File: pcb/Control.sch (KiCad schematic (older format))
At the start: 23 parts, among them SW1 Pulsador_2p, U1 ATMEGA328, U2 PCA9685, U3 FT231X, Y1 16MHz

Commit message: añadidos led para estado y alimentacion externa para salidas digitales
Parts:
- added D33, D34, D35: Rojo, Leds:LED_0805, symbol LED
- added R49, R50, R51: 270, Resistors_SMD:R_0805, symbol R
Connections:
- net +5V: now also D33.2 (A), D34.2 (A), D35.2 (A)
- net MISO: now also R50.1
- net MOSI: now also R49.1
- net SCK: now also R51.1
- new net: D33.1 (K), R49.2
- new net: D34.1 (K), R50.2
- new net: D35.1 (K), R51.2
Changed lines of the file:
@@
 Text GLabel 4250 3550 2    60   BiDi ~ 0
 MISO
-Text GLabel 4250 3650 2    60   Input ~ 0
+Text GLabel 4250 3650 2    60   BiDi ~ 0
 SCK
 Wire Wire Line
@@
 	1    0    0    -1
 $EndComp
+$Comp
+L LED D33
+U 1 1 57B391B3
+P 9500 5400
+F 0 "D33" V 9500 5600 50  0000 R CNN
+F 1 "Rojo" H 9750 5350 50  0000 R CNN
+F 2 "Leds:LED_0805" H 9500 5400 50  0001 C CNN
+F 3 "" H 9500 5400 50  0000 C CNN
+F 4 "KINGBRIGHT ELECTRONIC" H 1200 3750 60  0001 C CNN "Fabricante"
+F 5 "KP-2012EC" H 1200 3750 60  0001 C CNN "Ref"
+F 6 "~" H 1200 3750 60  0001 C CNN "Potencia"
+F 7 "~" H 1200 3750 60  0001 C CNN "Tolerancia"
+F 8 "tme" H 1200 3750 60  0001 C CNN "Provedor"
+F 9 "KP-2012EC" H 1200 3750 60  0001 C CNN "Ref_Proveedor"
+	1    9500 5400
+	0    -1   -1   0
+$EndComp
+$Comp
+L LED D34
+U 1 1 57B391C0
+P 9800 5400
+F 0 "D34" V 9800 5600 50  0000 R CNN
+F 1 "Rojo" H 10050 5350 50  0000 R CNN
+F 2 "Leds:LED_0805" H 9800 5400 50  0001 C CNN
+F 3 "" H 9800 5400 50  0000 C CNN
+F 4 "KINGBRIGHT ELECTRONIC" H 1300 3750 60  0001 C CNN "Fabricante"
+F 5 "KP-2012EC" H 1300 3750 60  0001 C CNN "Ref"
+F 6 "~" H 1300 3750 60  0001 C CNN "Potencia"
+F 7 "~" H 1300 3750 60  0001 C CNN "Tolerancia"
+F 8 "tme" H 1300 3750 60  0001 C CNN "Provedor"
+F 9 "KP-2012EC" H 1300 3750 60  0001 C CNN "Ref_Proveedor"
+	1    9800 5400
+	0    -1   -1   0
+$EndComp
+Wire Wire Line
+	9800 5600 9800 5900
+Wire Wire Line
+	9500 5800 9500 5600
+$Comp
+L +5V #PWR018
+U 1 1 57B391C9
+P 9500 4950
+F 0 "#PWR018" H 9500 4800 50  0001 C CNN
+F 1 "+5V" H 9515 5123 50  0000 C CNN
+F 2 "" H 9500 4950 50  0000 C CNN
+F 3 "" H 9500 4950 50  0000 C CNN
+	1    9500 4950
+	1    0    0    -1
+$EndComp
+$Comp
+L +5V #PWR019
+U 1 1 57B391CF
+P 9800 4950
+F 0 "#PWR019" H 9800 4800 50  0001 C CNN
+F 1 "+5V" H 9815 5123 50  0000 C CNN
+F 2 "" H 9800 4950 50  0000 C CNN
+F 3 "" H 9800 4950 50  0000 C CNN
+	1    9800 4950
+	1    0    0    -1
+$EndComp
+Wire Wire Line
+	9800 4950 9800 5200
+Wire Wire Line
+	9500 4950 9500 5200
+$Comp
+L R R50
+U 1 1 57B3920F
+P 8900 5900
+F 0 "R50" V 8950 5700 50  0000 C CNN
+F 1 "270" V 8900 5900 50  0000 C CNN
+F 2 "Resistors_SMD:R_0805" V 8830 5900 50  0001 C CNN
+F 3 "" H 8900 5900 50  0000 C CNN
+F 4 "vishay" H 1150 3850 60  0001 C CNN "Fabricante"
+F 5 "CRCW0805270RFKTABC" H 1150 3850 60  0001 C CNN "Ref"
+F 6 "~" H 1150 3850 60  0001 C CNN "Potencia"
+F 7 "~" H 1150 3850 60  0001 C CNN "Tolerancia"
+F 8 "tme" H 1150 3850 60  0001 C CNN "Provedor"
+F 9 "CRCW0805270RFKTABC" H 1150 3850 60  0001 C CNN "Ref_Proveedor"
+	1    8900 5900
+	0    -1   -1   0
+$EndComp
+$Comp
+L R R49
+U 1 1 57B3937B
+P 8550 5800
+F 0 "R49" V 8600 5600 50  0000 C CNN
+F 1 "270" V 8550 5800 50  0000 C CNN
+F 2 "Resistors_SMD:R_0805" V 8480 5800 50  0001 C CNN
+F 3 "" H 8550 5800 50  0000 C CNN
+F 4 "vishay" H 800 3750 60  0001 C CNN "Fabricante"
+F 5 "CRCW0805270RFKTABC" H 800 3750 60  0001 C CNN "Ref"
+F 6 "~" H 800 3750 60  0001 C CNN "Potencia"
+F 7 "~" H 800 3750 60  0001 C CNN "Tolerancia"
+F 8 "tme" H 800 3750 60  0001 C CNN "Provedor"
+F 9 "CRCW0805270RFKTABC" H 800 3750 60  0001 C CNN "Ref_Proveedor"
+	1    8550 5800
+	0    -1   -1   0
+$EndComp
+Wire Wire Line
+	8700 5800 9500 5800
+Wire Wire Line
+	9800 5900 9050 5900
+Text GLabel 8100 5800 0    60   BiDi ~ 0
+MOSI
+Text GLabel 8100 5900 0    60   BiDi ~ 0
+MISO
+Wire Wire Line
+	8100 5900 8750 5900
+Wire Wire Line
+	8400 5800 8100 5800
+$Comp
+L LED D35
+U 1 1 57B39D33
+P 10100 5400
+F 0 "D35" V 10100 5600 50  0000 R CNN
+F 1 "Rojo" H 10350 5350 50  0000 R CNN
+F 2 "Leds:LED_0805" H 10100 5400 50  0001 C CNN
+F 3 "" H 10100 5400 50  0000 C CNN
+F 4 "KINGBRIGHT ELECTRONIC" H 1600 3750 60  0001 C CNN "Fabricante"
+F 5 "KP-2012EC" H 1600 3750 60  0001 C CNN "Ref"
+F 6 "~" H 1600 3750 60  0001 C CNN "Potencia"
+F 7 "~" H 1600 3750 60  0001 C CNN "Tolerancia"
+F 8 "tme" H 1600 3750 60  0001 C CNN "Provedor"
+F 9 "KP-2012EC" H 1600 3750 60  0001 C CNN "Ref_Proveedor"
+	1    10100 5400
+	0    -1   -1   0
+$EndComp
+Wire Wire Line
+	10100 5600 10100 6000
+$Comp
+L +5V #PWR020
+U 1 1 57B39D3B
+P 10100 4950
+F 0 "#PWR020" H 10100 4800 50  0001 C CNN
+F 1 "+5V" H 10115 5123 50  0000 C CNN
+F 2 "" H 10100 4950 50  0000 C CNN
+F 3 "" H 10100 4950 50  0000 C CNN
+	1    10100 4950
+	1    0    0    -1
+$EndComp
+Wire Wire Line
+	10100 4950 10100 5200
+$Comp
+L R R51
+U 1 1 57B3A35F
+P 9250 6000
+F 0 "R51" V 9300 5800 50  0000 C CNN
+F 1 "270" V 9250 6000 50  0000 C CNN
+F 2 "Resistors_SMD:R_0805" V 9180 6000 50  0001 C CNN
+F 3 "" H 9250 6000 50  0000 C CNN
+F 4 "vishay" H 1500 3950 60  0001 C CNN "Fabricante"
+F 5 "CRCW0805270RFKTABC" H 1500 3950 60  0001 C CNN "Ref"
+F 6 "~" H 1500 3950 60  0001 C CNN "Potencia"
+F 7 "~" H 1500 3950 60  0001 C CNN "Tolerancia"
+F 8 "tme" H 1500 3950 60  0001 C CNN "Provedor"
+F 9 "CRCW0805270RFKTABC" H 1500 3950 60  0001 C CNN "Ref_Proveedor"
+	1    9250 6000
+	0    -1   -1   0
+$EndComp
+Text GLabel 8100 6000 0    60   BiDi ~ 0
+SCK
+Wire Wire Line
+	8100 6000 9100 6000
+Wire Wire Line
+	10100 6000 9400 6000
 $EndSCHEMATC

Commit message: añadir imagenes y datos al esquema electrico
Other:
- moved on the sheet: C1, C2, R1, R5, R6, SW1, U1, Y1

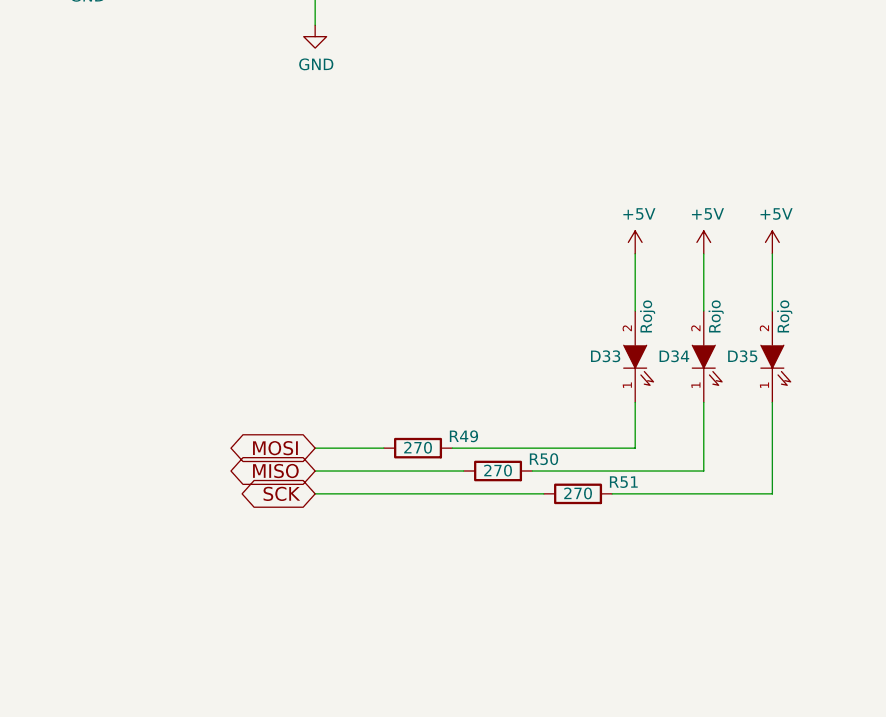
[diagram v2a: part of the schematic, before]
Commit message: correcciones menores y ecualizar longitud de pistas
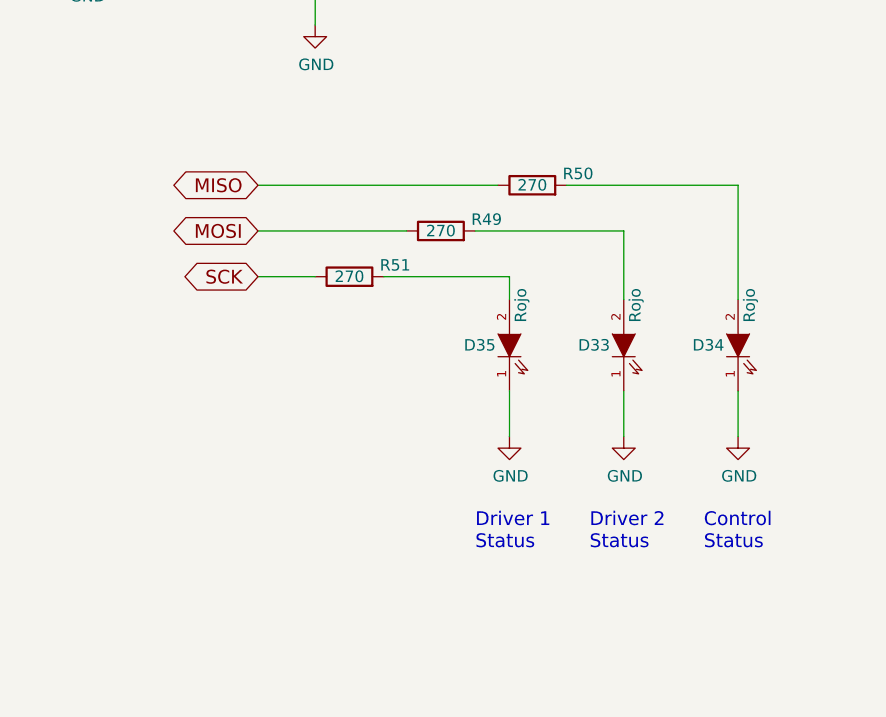
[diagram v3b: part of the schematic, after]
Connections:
- net +5V: no longer D33.2 (A), D34.2 (A), D35.2 (A)
- net GND: now also D33.1 (K), D34.1 (K), D35.1 (K)
- net at R49.2: now also D33.2 (A); no longer D33.1 (K)
- net at R50.2: now also D34.2 (A); no longer D34.1 (K)
- net at R51.2: now also D35.2 (A); no longer D35.1 (K)
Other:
- note added: "Control \nStatus"
- note added: "Driver 1 \nStatus"
- note added: "Driver 2 \nStatus"
- moved on the sheet: D33, D34, D35, R49, R50, R51
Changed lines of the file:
@@
-$EndComp
-$Comp
-L LED D33
-U 1 1 57B391B3
-P 9500 5400
-F 0 "D33" V 9500 5600 50  0000 R CNN
-F 1 "Rojo" H 9750 5350 50  0000 R CNN
-F 2 "Leds:LED_0805" H 9500 5400 50  0001 C CNN
-F 3 "" H 9500 5400 50  0000 C CNN
-F 4 "KINGBRIGHT ELECTRONIC" H 1200 3750 60  0001 C CNN "Fabricante"
-F 5 "KP-2012EC" H 1200 3750 60  0001 C CNN "Ref"
-F 6 "~" H 1200 3750 60  0001 C CNN "Potencia"
-F 7 "~" H 1200 3750 60  0001 C CNN "Tolerancia"
-F 8 "tme" H 1200 3750 60  0001 C CNN "Provedor"
-F 9 "KP-2012EC" H 1200 3750 60  0001 C CNN "Ref_Proveedor"
-	1    9500 5400
-	0    -1   -1   0
 $EndComp
 $Comp
 L LED D34
 U 1 1 57B391C0
-P 9800 5400
-F 0 "D34" V 9800 5600 50  0000 R CNN
-F 1 "Rojo" H 10050 5350 50  0000 R CNN
-F 2 "Leds:LED_0805" H 9800 5400 50  0001 C CNN
-F 3 "" H 9800 5400 50  0000 C CNN
-F 4 "KINGBRIGHT ELECTRONIC" H 1300 3750 60  0001 C CNN "Fabricante"
-F 5 "KP-2012EC" H 1300 3750 60  0001 C CNN "Ref"
-F 6 "~" H 1300 3750 60  0001 C CNN "Potencia"
-F 7 "~" H 1300 3750 60  0001 C CNN "Tolerancia"
-F 8 "tme" H 1300 3750 60  0001 C CNN "Provedor"
-F 9 "KP-2012EC" H 1300 3750 60  0001 C CNN "Ref_Proveedor"
-	1    9800 5400
+P 9950 5350
+F 0 "D34" V 9950 5550 50  0000 R CNN
+F 1 "Rojo" H 10200 5300 50  0000 R CNN
+F 2 "Leds:LED_0805" H 9950 5350 50  0001 C CNN
+F 3 "" H 9950 5350 50  0000 C CNN
+F 4 "KINGBRIGHT ELECTRONIC" H 1450 3700 60  0001 C CNN "Fabricante"
+F 5 "KP-2012EC" H 1450 3700 60  0001 C CNN "Ref"
+F 6 "~" H 1450 3700 60  0001 C CNN "Potencia"
+F 7 "~" H 1450 3700 60  0001 C CNN "Tolerancia"
+F 8 "tme" H 1450 3700 60  0001 C CNN "Provedor"
+F 9 "KP-2012EC" H 1450 3700 60  0001 C CNN "Ref_Proveedor"
+	1    9950 5350
 	0    -1   -1   0
 $EndComp
-Wire Wire Line
-	9800 5600 9800 5900
-Wire Wire Line
-	9500 5800 9500 5600
-$Comp
-L +5V #PWR018
-U 1 1 57B391C9
-P 9500 4950
-F 0 "#PWR018" H 9500 4800 50  0001 C CNN
-F 1 "+5V" H 9515 5123 50  0000 C CNN
-F 2 "" H 9500 4950 50  0000 C CNN
-F 3 "" H 9500 4950 50  0000 C CNN
-	1    9500 4950
-	1    0    0    -1
-$EndComp
-$Comp
-L +5V #PWR019
-U 1 1 57B391CF
-P 9800 4950
-F 0 "#PWR019" H 9800 4800 50  0001 C CNN
-F 1 "+5V" H 9815 5123 50  0000 C CNN
-F 2 "" H 9800 4950 50  0000 C CNN
-F 3 "" H 9800 4950 50  0000 C CNN
-	1    9800 4950
-	1    0    0    -1
-$EndComp
-Wire Wire Line
-	9800 4950 9800 5200
-Wire Wire Line
-	9500 4950 9500 5200
 $Comp
 L R R50
 U 1 1 57B3920F
-P 8900 5900
-F 0 "R50" V 8950 5700 50  0000 C CNN
-F 1 "270" V 8900 5900 50  0000 C CNN
-F 2 "Resistors_SMD:R_0805" V 8830 5900 50  0001 C CNN
-F 3 "" H 8900 5900 50  0000 C CNN
-F 4 "vishay" H 1150 3850 60  0001 C CNN "Fabricante"
-F 5 "CRCW0805270RFKTABC" H 1150 3850 60  0001 C CNN "Ref"
-F 6 "~" H 1150 3850 60  0001 C CNN "Potencia"
-F 7 "~" H 1150 3850 60  0001 C CNN "Tolerancia"
-F 8 "tme" H 1150 3850 60  0001 C CNN "Provedor"
-F 9 "CRCW0805270RFKTABC" H 1150 3850 60  0001 C CNN "Ref_Proveedor"
-	1    8900 5900
+P 9050 4650
+F 0 "R50" V 9100 4450 50  0000 C CNN
+F 1 "270" V 9050 4650 50  0000 C CNN
+F 2 "Resistors_SMD:R_0805" V 8980 4650 50  0001 C CNN
+F 3 "" H 9050 4650 50  0000 C CNN
+F 4 "vishay" H 1300 2600 60  0001 C CNN "Fabricante"
+F 5 "CRCW0805270RFKTABC" H 1300 2600 60  0001 C CNN "Ref"
+F 6 "~" H 1300 2600 60  0001 C CNN "Potencia"
+F 7 "~" H 1300 2600 60  0001 C CNN "Tolerancia"
+F 8 "tme" H 1300 2600 60  0001 C CNN "Provedor"
+F 9 "CRCW0805270RFKTABC" H 1300 2600 60  0001 C CNN "Ref_Proveedor"
+	1    9050 4650
 	0    -1   -1   0
 $EndComp
@@
 L R R49
 U 1 1 57B3937B
-P 8550 5800
-F 0 "R49" V 8600 5600 50  0000 C CNN
-F 1 "270" V 8550 5800 50  0000 C CNN
-F 2 "Resistors_SMD:R_0805" V 8480 5800 50  0001 C CNN
-F 3 "" H 8550 5800 50  0000 C CNN
-F 4 "vishay" H 800 3750 60  0001 C CNN "Fabricante"
-F 5 "CRCW0805270RFKTABC" H 800 3750 60  0001 C CNN "Ref"
-F 6 "~" H 800 3750 60  0001 C CNN "Potencia"
-F 7 "~" H 800 3750 60  0001 C CNN "Tolerancia"
-F 8 "tme" H 800 3750 60  0001 C CNN "Provedor"
-F 9 "CRCW0805270RFKTABC" H 800 3750 60  0001 C CNN "Ref_Proveedor"
-	1    8550 5800
+P 8650 4850
+F 0 "R49" V 8700 4650 50  0000 C CNN
+F 1 "270" V 8650 4850 50  0000 C CNN
+F 2 "Resistors_SMD:R_0805" V 8580 4850 50  0001 C CNN
+F 3 "" H 8650 4850 50  0000 C CNN
+F 4 "vishay" H 900 2800 60  0001 C CNN "Fabricante"
+F 5 "CRCW0805270RFKTABC" H 900 2800 60  0001 C CNN "Ref"
+F 6 "~" H 900 2800 60  0001 C CNN "Potencia"
+F 7 "~" H 900 2800 60  0001 C CNN "Tolerancia"
+F 8 "tme" H 900 2800 60  0001 C CNN "Provedor"
+F 9 "CRCW0805270RFKTABC" H 900 2800 60  0001 C CNN "Ref_Proveedor"
+	1    8650 4850
 	0    -1   -1   0
 $EndComp
-Wire Wire Line
-	8700 5800 9500 5800
-Wire Wire Line
-	9800 5900 9050 5900
-Text GLabel 8100 5800 0    60   BiDi ~ 0
+Text GLabel 7850 4850 0    60   BiDi ~ 0
 MOSI
-Text GLabel 8100 5900 0    60   BiDi ~ 0
+Text GLabel 7850 4650 0    60   BiDi ~ 0
 MISO
 Wire Wire Line
-	8100 5900 8750 5900
-Wire Wire Line
-	8400 5800 8100 5800
+	7850 4650 8900 4650
 $Comp
 L LED D35
 U 1 1 57B39D33
-P 10100 5400
-F 0 "D35" V 10100 5600 50  0000 R CNN
-F 1 "Rojo" H 10350 5350 50  0000 R CNN
-F 2 "Leds:LED_0805" H 10100 5400 50  0001 C CNN
-F 3 "" H 10100 5400 50  0000 C CNN
-F 4 "KINGBRIGHT ELECTRONIC" H 1600 3750 60  0001 C CNN "Fabricante"
-F 5 "KP-2012EC" H 1600 3750 60  0001 C CNN "Ref"
-F 6 "~" H 1600 3750 60  0001 C CNN "Potencia"
-F 7 "~" H 1600 3750 60  0001 C CNN "Tolerancia"
-F 8 "tme" H 1600 3750 60  0001 C CNN "Provedor"
-F 9 "KP-2012EC" H 1600 3750 60  0001 C CNN "Ref_Proveedor"
-	1    10100 5400
+P 8950 5350
+F 0 "D35" V 8950 5550 50  0000 R CNN
+F 1 "Rojo" H 9200 5300 50  0000 R CNN
+F 2 "Leds:LED_0805" H 8950 5350 50  0001 C CNN
+F 3 "" H 8950 5350 50  0000 C CNN
+F 4 "KINGBRIGHT ELECTRONIC" H 450 3700 60  0001 C CNN "Fabricante"
+F 5 "KP-2012EC" H 450 3700 60  0001 C CNN "Ref"
+F 6 "~" H 450 3700 60  0001 C CNN "Potencia"
+F 7 "~" H 450 3700 60  0001 C CNN "Tolerancia"
+F 8 "tme" H 450 3700 60  0001 C CNN "Provedor"
+F 9 "KP-2012EC" H 450 3700 60  0001 C CNN "Ref_Proveedor"
+	1    8950 5350
 	0    -1   -1   0
 $EndComp
-Wire Wire Line
-	10100 5600 10100 6000
-$Comp
-L +5V #PWR020
-U 1 1 57B39D3B
-P 10100 4950
-F 0 "#PWR020" H 10100 4800 50  0001 C CNN
-F 1 "+5V" H 10115 5123 50  0000 C CNN
-F 2 "" H 10100 4950 50  0000 C CNN
-F 3 "" H 10100 4950 50  0000 C CNN
-	1    10100 4950
-	1    0    0    -1
-$EndComp
-Wire Wire Line
-	10100 4950 10100 5200
 $Comp
 L R R51
 U 1 1 57B3A35F
-P 9250 6000
-F 0 "R51" V 9300 5800 50  0000 C CNN
-F 1 "270" V 9250 6000 50  0000 C CNN
-F 2 "Resistors_SMD:R_0805" V 9180 6000 50  0001 C CNN
-F 3 "" H 9250 6000 50  0000 C CNN
-F 4 "vishay" H 1500 3950 60  0001 C CNN "Fabricante"
-F 5 "CRCW0805270RFKTABC" H 1500 3950 60  0001 C CNN "Ref"
-F 6 "~" H 1500 3950 60  0001 C CNN "Potencia"
-F 7 "~" H 1500 3950 60  0001 C CNN "Tolerancia"
-F 8 "tme" H 1500 3950 60  0001 C CNN "Provedor"
-F 9 "CRCW0805270RFKTABC" H 1500 3950 60  0001 C CNN "Ref_Proveedor"
-	1    9250 6000
+P 8250 5050
+F 0 "R51" V 8300 4850 50  0000 C CNN
+F 1 "270" V 8250 5050 50  0000 C CNN
+F 2 "Resistors_SMD:R_0805" V 8180 5050 50  0001 C CNN
+F 3 "" H 8250 5050 50  0000 C CNN
+F 4 "vishay" H 500 3000 60  0001 C CNN "Fabricante"
+F 5 "CRCW0805270RFKTABC" H 500 3000 60  0001 C CNN "Ref"
+F 6 "~" H 500 3000 60  0001 C CNN "Potencia"
+F 7 "~" H 500 3000 60  0001 C CNN "Tolerancia"
+F 8 "tme" H 500 3000 60  0001 C CNN "Provedor"
+F 9 "CRCW0805270RFKTABC" H 500 3000 60  0001 C CNN "Ref_Proveedor"
+	1    8250 5050
 	0    -1   -1   0
 $EndComp
-Text GLabel 8100 6000 0    60   BiDi ~ 0
+Text GLabel 7850 5050 0    60   BiDi ~ 0
 SCK
-Wire Wire Line
-	8100 6000 9100 6000
-Wire Wire Line
-	10100 6000 9400 6000
 $Bitmap
 Pos 10900 6850
@@
 EndData
 $EndBitmap
+Wire Wire Line
+	8100 5050 7850 5050
+$Comp
+L LED D33
+U 1 1 57B391B3
+P 9450 5350
+F 0 "D33" V 9450 5550 50  0000 R CNN
+F 1 "Rojo" H 9700 5300 50  0000 R CNN
+F 2 "Leds:LED_0805" H 9450 5350 50  0001 C CNN
+F 3 "" H 9450 5350 50  0000 C CNN
+F 4 "KINGBRIGHT ELECTRONIC" H 1150 3700 60  0001 C CNN "Fabricante"
+F 5 "KP-2012EC" H 1150 3700 60  0001 C CNN "Ref"
+F 6 "~" H 1150 3700 60  0001 C CNN "Potencia"
+F 7 "~" H 1150 3700 60  0001 C CNN "Tolerancia"
+F 8 "tme" H 1150 3700 60  0001 C CNN "Provedor"
+F 9 "KP-2012EC" H 1150 3700 60  0001 C CNN "Ref_Proveedor"
+	1    9450 5350
+	0    -1   -1   0
+$EndComp
+$Comp
+L GND #PWR018
+U 1 1 57B5BB38
+P 9450 5750
+F 0 "#PWR018" H 9450 5500 50  0001 C CNN
+F 1 "GND" H 9455 5577 50  0000 C CNN
+F 2 "" H 9450 5750 50  0000 C CNN
+F 3 "" H 9450 5750 50  0000 C CNN
+	1    9450 5750
+	1    0    0    -1
+$EndComp
+$Comp
+L GND #PWR019
+U 1 1 57B5BBA1
+P 9950 5750
+F 0 "#PWR019" H 9950 5500 50  0001 C CNN
+F 1 "GND" H 9955 5577 50  0000 C CNN
+F 2 "" H 9950 5750 50  0000 C CNN
+F 3 "" H 9950 5750 50  0000 C CNN
+	1    9950 5750
+	1    0    0    -1
+$EndComp
+$Comp
+L GND #PWR020
+U 1 1 57B5BC03
+P 8950 5750
+F 0 "#PWR020" H 8950 5500 50  0001 C CNN
+F 1 "GND" H 8955 5577 50  0000 C CNN
+F 2 "" H 8950 5750 50  0000 C CNN
+F 3 "" H 8950 5750 50  0000 C CNN
+	1    8950 5750
+	1    0    0    -1
+$EndComp
+Wire Wire Line
+	8950 5550 8950 5750
+Wire Wire Line
+	9450 5550 9450 5750
+Wire Wire Line
+	7850 4850 8500 4850
+Wire Wire Line
+	9200 4650 9950 4650
+Wire Wire Line
+	9950 4650 9950 5150
+Wire Wire Line
+	9950 5550 9950 5750
+Wire Wire Line
+	8800 4850 9450 4850
+Wire Wire Line
+	9450 4850 9450 5150
+Wire Wire Line
+	8950 5150 8950 5050
+Wire Wire Line
+	8950 5050 8400 5050
+Text Notes 9800 6250 0    60   ~ 0
+Control \nStatus
+Text Notes 9300 6250 0    60   ~ 0
+Driver 2 \nStatus
+Text Notes 8800 6250 0    60   ~ 0
+Driver 1 \nStatus
 $EndSCHEMATC
